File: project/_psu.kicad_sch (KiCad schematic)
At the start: 40 parts, among them J201 5V, J202 24V, J203 3V3, U201 DP9700AT-24, U202 ME3121AM6G, U203 JTD6206-3.3V

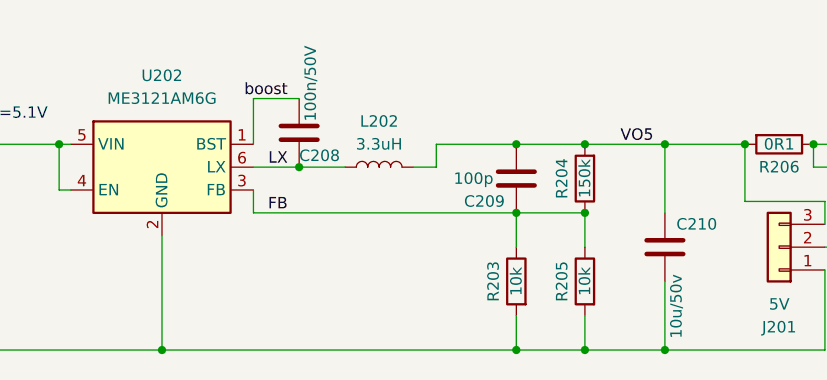
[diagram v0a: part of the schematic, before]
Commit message: fix PSU FB and tmp102 pinout
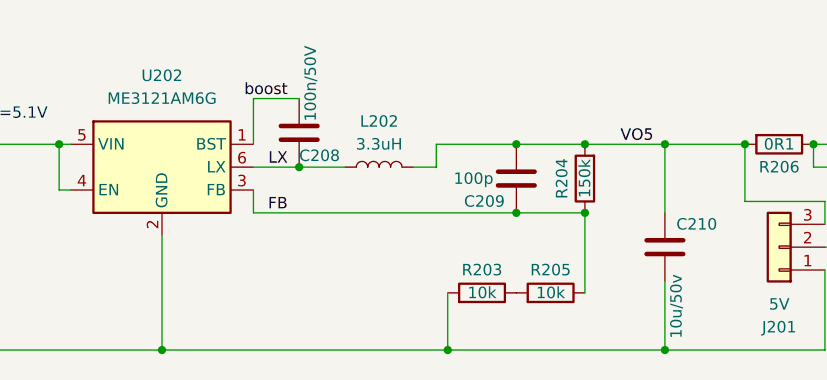
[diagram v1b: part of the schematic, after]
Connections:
- net FB: no longer R203.1
- net GND: no longer R205.2
- new net: R203.1, R205.2
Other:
- moved on the sheet: R203, R205
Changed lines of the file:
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@@
   (junction (at 212.09 63.5) (diameter 0) (color 0 0 0 0)
   )
+  (junction (at 124.46 127) (diameter 0) (color 0 0 0 0)
+  )
   (junction (at 207.01 55.88) (diameter 0) (color 0 0 0 0)
   )
@@
   (junction (at 74.93 45.72) (diameter 0) (color 0 0 0 0)
   )
-  (junction (at 132.08 127) (diameter 0) (color 0 0 0 0)
-  )
   (junction (at 203.2 55.88) (diameter 0) (color 0 0 0 0)
   )
@@
   (junction (at 234.95 127) (diameter 0) (color 0 0 0 0)
   )
-  (junction (at 139.7 127) (diameter 0) (color 0 0 0 0)
-  )
   (junction (at 139.7 111.76) (diameter 0) (color 0 0 0 0)
   )
@@
     (stroke (width 0) (type default) (color 0 0 0 0))
   )
-  (wire (pts (xy 92.71 127) (xy 132.08 127))
+  (wire (pts (xy 92.71 127) (xy 124.46 127))
     (stroke (width 0) (type default) (color 0 0 0 0))
   )
@@
     (stroke (width 0) (type default) (color 0 0 0 0))
   )
+  (wire (pts (xy 124.46 120.65) (xy 124.46 127))
+    (stroke (width 0) (type default) (color 0 0 0 0))
+  )
   (wire (pts (xy 166.37 118.11) (xy 166.37 127))
     (stroke (width 0) (type default) (color 0 0 0 0))
@@
     (stroke (width 0) (type default) (color 0 0 0 0))
   )
-  (wire (pts (xy 139.7 115.57) (xy 139.7 111.76))
+  (wire (pts (xy 139.7 111.76) (xy 139.7 120.65))
     (stroke (width 0) (type default) (color 0 0 0 0))
   )
@@
     (stroke (width 0) (type default) (color 0 0 0 0))
   )
-  (wire (pts (xy 132.08 127) (xy 139.7 127))
-    (stroke (width 0) (type default) (color 0 0 0 0))
-  )
   (wire (pts (xy 208.28 127) (xy 223.52 127))
     (stroke (width 0) (type default) (color 0 0 0 0))
@@
     (stroke (width 0) (type default) (color 0 0 0 0))
   )
-  (wire (pts (xy 132.08 111.76) (xy 132.08 115.57))
-    (stroke (width 0) (type default) (color 0 0 0 0))
-  )
-  (wire (pts (xy 139.7 123.19) (xy 139.7 127))
-    (stroke (width 0) (type default) (color 0 0 0 0))
-  )
   (wire (pts (xy 123.19 104.14) (xy 132.08 104.14))
     (stroke (width 0) (type default) (color 0 0 0 0))
@@
     (stroke (width 0) (type default) (color 0 0 0 0))
   )
+  (wire (pts (xy 124.46 127) (xy 148.59 127))
+    (stroke (width 0) (type default) (color 0 0 0 0))
+  )
   (wire (pts (xy 81.28 104.14) (xy 81.28 109.22))
     (stroke (width 0) (type default) (color 0 0 0 0))
@@
     (stroke (width 0) (type default) (color 0 0 0 0))
   )
-  (wire (pts (xy 132.08 123.19) (xy 132.08 127))
-    (stroke (width 0) (type default) (color 0 0 0 0))
-  )
   (wire (pts (xy 212.09 63.5) (xy 236.22 63.5))
     (stroke (width 0) (type default) (color 0 0 0 0))
@@
   )
   (wire (pts (xy 208.28 104.14) (xy 208.28 105.41))
-    (stroke (width 0) (type default) (color 0 0 0 0))
-  )
-  (wire (pts (xy 139.7 127) (xy 148.59 127))
     (stroke (width 0) (type default) (color 0 0 0 0))
   )
@@
     (pin "2")
   )
-  (symbol (lib_id "Device:R") (at 139.7 119.38 0) (mirror y) (unit 1)
-    (in_bom yes) (on_board yes)
-    (property "Reference" "R205" (id 0) (at 137.16 119.38 90))
-    (property "Value" "10k" (id 1) (at 139.7 119.38 90))
-    (property "Footprint" "Resistor_SMD:R_0805_2012Metric_Pad1.20x1.40mm_HandSolder" (id 2) (at 141.478 119.38 90)
-      (effects (font (size 1.27 1.27)) hide)
-    )
-    (property "Datasheet" "~" (id 3) (at 139.7 119.38 0)
-      (effects (font (size 1.27 1.27)) hide)
-    )
-    (property "jlc-part-type" "B+" (id 4) (at 139.7 119.38 0)
-      (effects (font (size 1.27 1.27)) hide)
-    )
-    (property "lcsc#" "C17414" (id 5) (at 139.7 119.38 0)
+  (symbol (lib_id "Device:R") (at 135.89 120.65 270) (mirror x) (unit 1)
+    (in_bom yes) (on_board yes)
+    (property "Reference" "R205" (id 0) (at 135.89 118.11 90))
+    (property "Value" "10k" (id 1) (at 135.89 120.65 90))
+    (property "Footprint" "Resistor_SMD:R_0805_2012Metric_Pad1.20x1.40mm_HandSolder" (id 2) (at 135.89 122.428 90)
+      (effects (font (size 1.27 1.27)) hide)
+    )
+    (property "Datasheet" "~" (id 3) (at 135.89 120.65 0)
+      (effects (font (size 1.27 1.27)) hide)
+    )
+    (property "jlc-part-type" "B+" (id 4) (at 135.89 120.65 0)
+      (effects (font (size 1.27 1.27)) hide)
+    )
+    (property "lcsc#" "C17414" (id 5) (at 135.89 120.65 0)
       (effects (font (size 1.27 1.27)) hide)
     )
@@
     (pin "2")
   )
-  (symbol (lib_id "Device:R") (at 132.08 119.38 0) (mirror y) (unit 1)
-    (in_bom yes) (on_board yes)
-    (property "Reference" "R203" (id 0) (at 129.54 119.38 90))
-    (property "Value" "10k" (id 1) (at 132.08 119.38 90))
-    (property "Footprint" "Resistor_SMD:R_0805_2012Metric_Pad1.20x1.40mm_HandSolder" (id 2) (at 133.858 119.38 90)
-      (effects (font (size 1.27 1.27)) hide)
-    )
-    (property "Datasheet" "~" (id 3) (at 132.08 119.38 0)
-      (effects (font (size 1.27 1.27)) hide)
-    )
-    (property "jlc-part-type" "B+" (id 4) (at 132.08 119.38 0)
-      (effects (font (size 1.27 1.27)) hide)
-    )
-    (property "lcsc#" "C17414" (id 5) (at 132.08 119.38 0)
-      (effects (font (size 1.27 1.27)) hide)
-    )
+  (symbol (lib_id "Device:R") (at 128.27 120.65 270) (mirror x) (unit 1)
+    (in_bom yes) (on_board yes)
+    (property "Reference" "R203" (id 0) (at 128.27 118.11 90))
+    (property "Value" "10k" (id 1) (at 128.27 120.65 90))
+    (property "Footprint" "Resistor_SMD:R_0805_2012Metric_Pad1.20x1.40mm_HandSolder" (id 2) (at 128.27 122.428 90)
+      (effects (font (size 1.27 1.27)) hide)
+    )
+    (property "Datasheet" "~" (id 3) (at 128.27 120.65 0)
+      (effects (font (size 1.27 1.27)) hide)
+    )
+    (property "jlc-part-type" "B+" (id 4) (at 128.27 120.65 0)
+      (effects (font (size 1.27 1.27)) hide)
+    )
+    (property "lcsc#" "C17414" (id 5) (at 128.27 120.65 0)
+      (effects (font (size 1.27 1.27)) hide)
+    )
